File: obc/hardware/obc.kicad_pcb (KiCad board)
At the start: 4 copper layers, 80 x 80 mm, 104 parts, among them J1 Conn_ARM_JTAG_SWD_10, J2 Micro_SD_Card, J3 Conn_Coaxial, J4 USB_C_Receptacle_USB2.0_16P, J5 Conn_Coaxial, Q1 AO3401A, Q2 AO3400A, SW1 SW_SPDT, SW2 SW_Push, U1 STM32H743ZGT6, U10 LM66100DCK, U11 LM66100DCK, U12 USBLC6-2P6, U13 ISM6HG256X, U2 RFM96W-433S2, U3 MAX6369, U4 MAX-M10S, U5 FM24CL16B, U6 MS5607-02BA, U7 SN65HVD230, U8 SN65HVD230, U9 AMS1117-3.3, Y1 25 MHz, Y2 32.768 kHz

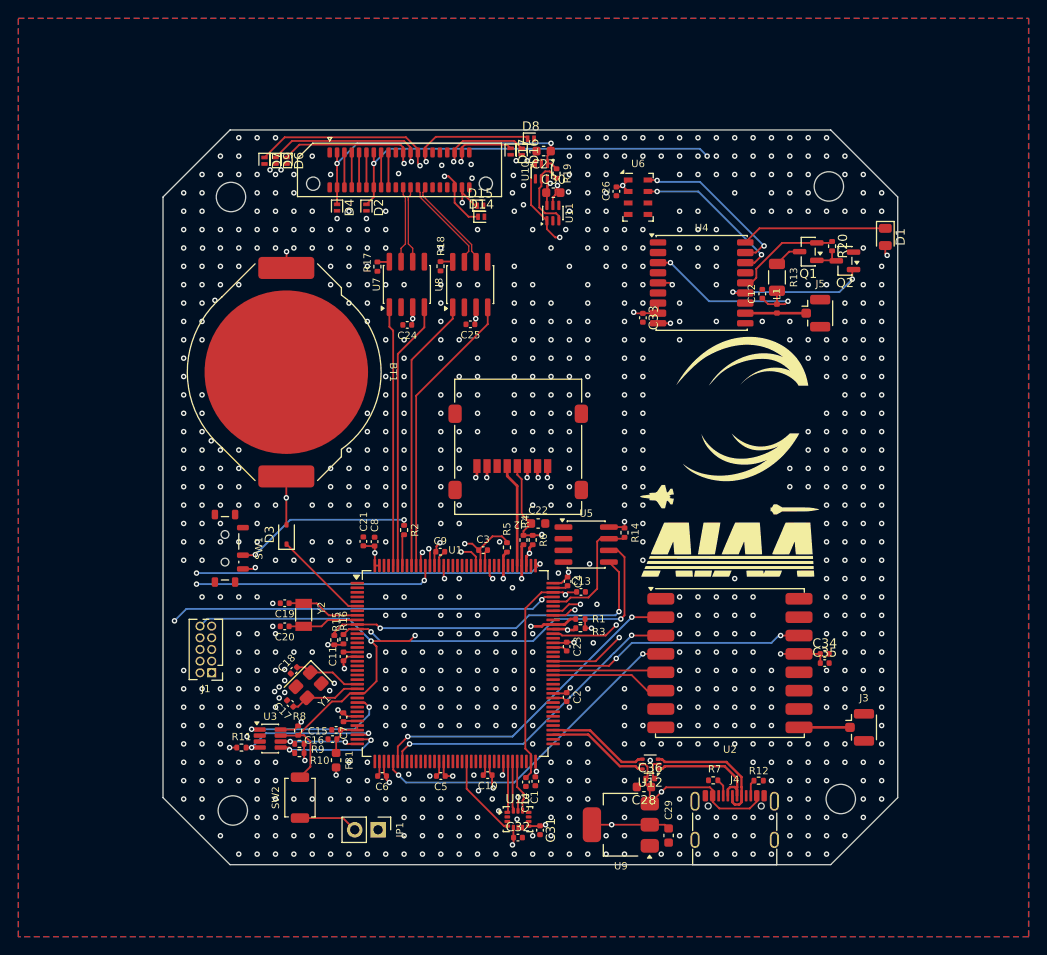
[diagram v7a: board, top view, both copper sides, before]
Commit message: added github QR code, fixed DRC violations, cleaned up silk
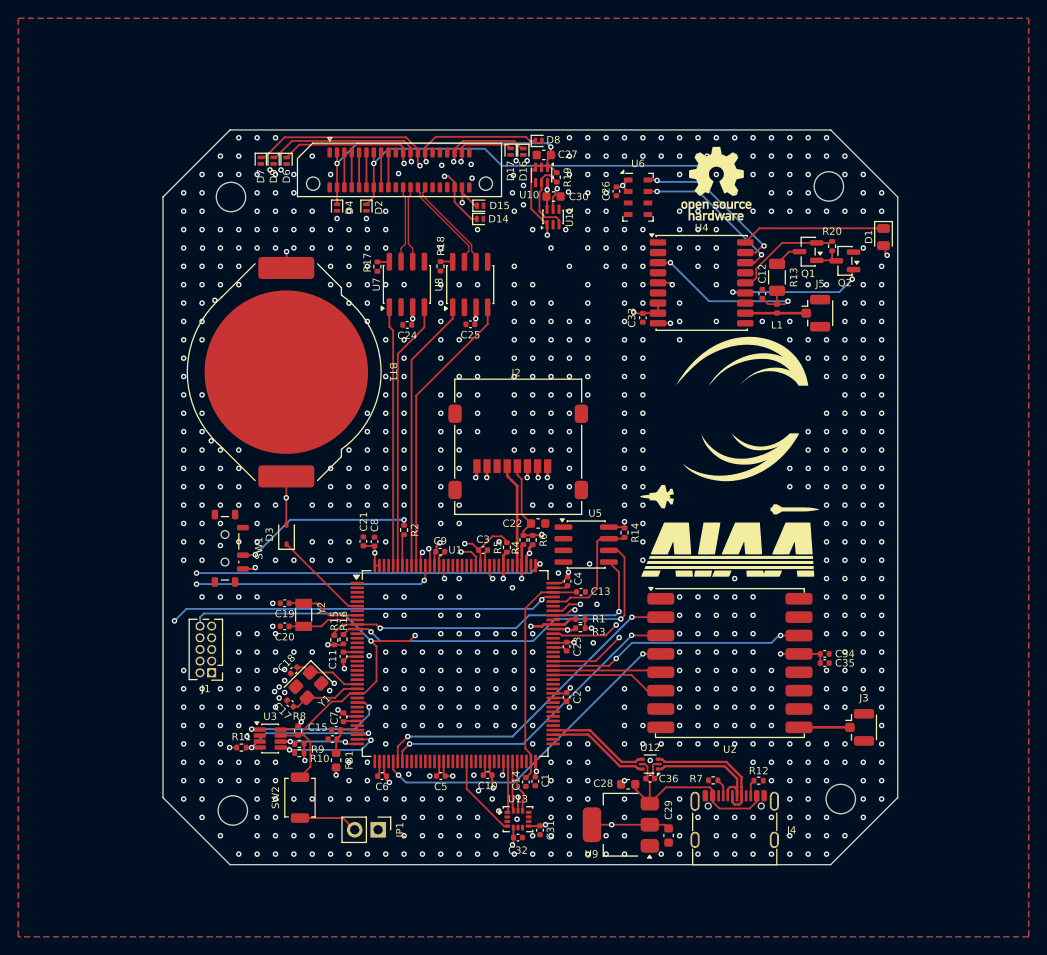
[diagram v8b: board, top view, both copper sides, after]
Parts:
- added REF**: OSHW-Logo_7.5x8mm_SilkScreen, Symbol:OSHW-Logo_7.5x8mm_SilkScreen, F.Cu at (151.0, 58.0)
- moved REF** 21.3 mm to (100.7, 113.5)
- moved C28 1.74 mm to (141.4, 123.4)
- moved D8 0.89 mm to (131.7, 53.3)
- moved C27 0.42 mm to (132.2, 54.9)
- moved C30 0.42 mm to (133.3, 59.4)
- moved R19 0.42 mm to (133.6, 57.3)
- moved U10 0.42 mm to (132.0, 57.1)
- moved U11 0.42 mm to (133.2, 61.6)
- moved D7 0.40 mm to (101.4, 55.5)
- moved D14 0.27 mm to (125.3, 61.8)
- moved D9 0.21 mm to (102.8, 55.5)
- moved D1 0.20 mm to (169.2, 63.8)
- moved D16 0.18 mm to (130.0, 54.5)
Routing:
- net VBUS: track 20.2 -> 22.8 mm, vias 1 -> 0
- net /STM32H7/~{RESET}: track 118.4 -> 119.7 mm
- net /Inter-Board-Connector/OBC_HEARTBEAT: track 57.5 -> 58.4 mm
- net VDD_RADIO: track 106.1 -> 107.0 mm
- net Net-(U10-~{CE}): track 84.6 -> 83.9 mm
- net +3V3: track 78.9 -> 78.3 mm
- net Net-(C13-Pad1): track 25.5 -> 25.2 mm, vias 1 -> 0
